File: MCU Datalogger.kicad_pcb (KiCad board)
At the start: 2 copper layers, 29 parts, among them J1 Conn_01x04_Pin, J2 Conn_01x04_Pin, J3 Conn_01x09_Pin, J4 Conn_02x03_Odd_Even, U1 24LC1025, U2 24LC1025, U3 DS1337S_, U4 ATMEGA328P-AU, Y1 32.768 KHz, Y2 16 MHz

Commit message: Completed placements of footprints.
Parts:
- moved H3 129.1 mm to (110.5, 38.1)
- moved C5 128.3 mm to (94.0, 38.1)
- moved R7 122.7 mm to (98.4, 41.9), turned to 180 degrees
- moved C3 121.6 mm to (89.5, 38.1)
- moved D2 120.5 mm to (102.9, 38.1)
- moved BT1 120.1 mm to (69.2, 43.9)
- moved R5 119.0 mm to (102.9, 41.9), turned to 180 degrees
- moved R6 118.2 mm to (102.9, 45.7)
- moved D1 116.6 mm to (98.7, 38.1)
- moved C1 115.0 mm to (85.1, 38.1)
- moved U3 112.5 mm to (77.4, 54.0)
- moved U4 112.4 mm to (89.5, 47.4)
- moved H4 112.4 mm to (110.5, 63.5)
- moved R4 111.0 mm to (98.4, 45.7)
- moved J4 110.8 mm to (107.3, 42.5)
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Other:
- board outline added: 49.3 x 30.5 mm

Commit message: routing sans GND Vcc complete.
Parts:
- moved BT1 0.64 mm to (68.6, 43.9)
- moved Y1 0.64 mm to (68.6, 54.7)
- moved U4 0.63 mm to (88.9, 47.4)
- moved R1 0.57 mm to (73.7, 59.1)
- moved R2 0.57 mm to (77.5, 59.1)
- moved U3 0.57 mm to (76.8, 54.0)
- moved U1 0.57 mm to (76.9, 47.0)
- moved U2 0.57 mm to (76.9, 40.0)
- turned C1 to 180 degrees
- turned C4 to 180 degrees
- turned Y2 to 180 degrees
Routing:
- net /Vcc: track 0.00 -> 130.9 mm, vias 0 -> 5
- net /SCK: track 0.00 -> 95.1 mm
- net /SDA: track 0.00 -> 60.0 mm, vias 0 -> 4
- net GND: track 0.00 -> 59.2 mm, vias 0 -> 5
- net Net-(BT1-+): track 0.00 -> 55.3 mm, vias 0 -> 2
- net /TX: track 0.00 -> 29.9 mm, vias 0 -> 1
- net /D2: track 0.00 -> 29.3 mm
- net /RX: track 0.00 -> 27.0 mm, vias 0 -> 1
- net /MOSI: track 0.00 -> 26.4 mm
- net Net-(U4-PB7): track 0.00 -> 25.2 mm, vias 0 -> 2
- net /MISO: track 0.00 -> 24.3 mm
- net /D3: track 0.00 -> 24.2 mm
- net /RESET: track 0.00 -> 22.7 mm, vias 0 -> 2
- net Net-(U4-PB6): track 0.00 -> 22.5 mm
- net /D4: track 0.00 -> 21.6 mm
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
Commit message: Completed routing.
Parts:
- moved H3 0.64 mm to (111.1, 38.1)
- moved H4 0.64 mm to (111.1, 63.5)
- moved H1 0.31 mm to (66.7, 38.1)
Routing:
- net GND: track 59.2 -> 62.9 mm, vias 5 -> 7
- added copper zone on B.Cu, net GND
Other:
- board size 49.3 x 30.5 mm -> 49.8 x 30.5 mm
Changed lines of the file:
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@@
 		(tags "resistor")
 		(property "Reference" "R5"
-			(at 0 -1.65 0)
+			(at 0.9125 1.81 0)
 			(layer "F.SilkS")
 			(effects
@@
 		(tags "resistor")
 		(property "Reference" "R3"
-			(at 0 -1.65 0)
+			(at -0.675 1.63 0)
 			(layer "F.SilkS")
 			(effects
@@
 		(tags "Through hole pin header THT 1x04 2.54mm single row")
 		(property "Reference" "J1"
-			(at 0 -2.38 0)
+			(at -2.655 -0.85 0)
 			(layer "F.SilkS")
 			(effects
@@
 		(tags "resistor")
 		(property "Reference" "R6"
-			(at 0 -1.65 0)
+			(at -0.615732 -1.92 0)
 			(layer "F.SilkS")
 			(effects
@@
 		(tags "Through hole pin header THT 2x03 2.54mm double row")
 		(property "Reference" "J4"
-			(at 1.27 -2.38 0)
+			(at 0.69 -2.38 0)
 			(layer "F.SilkS")
 			(effects
@@
 	(footprint "MountingHole:MountingHole_2.1mm"
 		(layer "F.Cu")
-		(at 110.49 38.1)
+		(at 111.125 38.1)
 		(descr "Mounting Hole 2.1mm, no annular, generated by kicad-footprint-generator mountinghole.py")
 		(tags "mountinghole")
 		(property "Reference" "H3"
-			(at 0 -3.05 0)
+			(at -3.49 -1.524 0)
 			(layer "F.SilkS")
 			(effects
@@
 		(tags "Through hole pin header THT 1x09 2.54mm single row")
 		(property "Reference" "J3"
-			(at 0 -2.38 90)
+			(at 0 -2.38 180)
 			(layer "F.SilkS")
 			(effects
@@
 	(footprint "MountingHole:MountingHole_2.1mm"
 		(layer "F.Cu")
-		(at 66.675 37.79)
+		(at 66.675 38.1)
 		(descr "Mounting Hole 2.1mm, no annular, generated by kicad-footprint-generator mountinghole.py")
 		(tags "mountinghole")
 		(property "Reference" "H1"
-			(at 0 -3.05 0)
+			(at -1.05 2.91 0)
 			(layer "F.SilkS")
 			(effects
@@
 		(tags "Through hole pin header THT 1x04 2.54mm single row")
 		(property "Reference" "J2"
-			(at 0 -2.38 90)
+			(at 0 -2.38 180)
 			(layer "F.SilkS")
 			(effects
@@
 		(descr "SMD2520/2, Crystal, 5.0x3.2mm package, SMD, hand-soldering, generated with kicad-footprint-generator make_crystal.py, http://www.icbase.com/File/PDF/HKC/HKC00061008.pdf")
 		(property "Reference" "Y1"
-			(at 0 -2.8 90)
+			(at -5.37 0.18 180)
 			(layer "F.SilkS")
 			(effects
@@
 	(footprint "MountingHole:MountingHole_2.1mm"
 		(layer "F.Cu")
-		(at 110.49 63.5)
+		(at 111.125 63.5)
 		(descr "Mounting Hole 2.1mm, no annular, generated by kicad-footprint-generator mountinghole.py")
 		(tags "mountinghole")
 		(property "Reference" "H4"
-			(at 0 -3.05 0)
+			(at -2.49 -2 0)
 			(layer "F.SilkS")
 			(effects
@@
 		(tags "capacitor")
 		(property "Reference" "C1"
-			(at 0 -1.68 0)
+			(at 0.45 1.8 0)
 			(layer "F.SilkS")
 			(effects
@@
 		(tags "SOIC SO P-SOP SOP SOP-8 SO SO-8 8S2 S2AE/F K04-056 CASE-751BE SO8W 8-Pin-SOIC PSA W8-2 W8-4 W8MS-1 FPT-8P-M08")
 		(property "Reference" "U1"
-			(at 0 -3.6 0)
+			(at 0 -3.39 0)
 			(layer "F.SilkS")
 			(effects
@@
 		(at 88.9 47.35)
 		(property "Reference" "U4"
-			(at -2.795 -6.79 0)
+			(at -2.795 -6.25 0)
 			(layer "F.SilkS")
 			(effects
@@
 		(tags "resistor")
 		(property "Reference" "R7"
-			(at 0 -1.65 0)
+			(at 0.4 1.91 0)
 			(layer "F.SilkS")
 			(effects
@@
 		(tags "resistor")
 		(property "Reference" "R4"
-			(at 0 -1.65 0)
+			(at -0.9125 -1.8075 0)
 			(layer "F.SilkS")
 			(effects
@@
 	(gr_rect
 		(start 64.135 35.433)
-		(end 113.411 65.913)
+		(end 113.919 65.913)
 		(stroke
 			(width 0.05)
@@
 	)
 	(segment
+		(start 84.73 46.15)
+		(end 85.886117 46.15)
+		(width 0.35)
+		(layer "F.Cu")
+		(net 1)
+	)
+	(segment
 		(start 84.77 39.37)
 		(end 86.04 38.1)
@@
 	)
 	(segment
+		(start 93.07 46.95)
+		(end 92.295912 46.95)
+		(width 0.35)
+		(layer "F.Cu")
+		(net 1)
+	)
+	(segment
 		(start 68.58 46.41)
 		(end 73.08 41.91)
@@
 	)
 	(segment
+		(start 91.6 46.254088)
+		(end 91.6 45.4)
+		(width 0.35)
+		(layer "F.Cu")
+		(net 1)
+	)
+	(segment
 		(start 74.93 39.37)
 		(end 80.4875 39.37)
@@
 	)
 	(segment
+		(start 92.295912 46.95)
+		(end 91.6 46.254088)
+		(width 0.35)
+		(layer "F.Cu")
+		(net 1)
+	)
+	(segment
 		(start 99.3375 40.3375)
 		(end 99.25 40.25)
@@
 	)
 	(via
+		(at 85.886117 46.15)
+		(size 0.9)
+		(drill 0.4)
+		(layers "F.Cu" "B.Cu")
+		(net 1)
+	)
+	(via
 		(at 96.15 38.05)
 		(size 0.9)
@@
 	)
 	(via
+		(at 91.6 45.4)
+		(size 0.9)
+		(drill 0.4)
+		(layers "F.Cu" "B.Cu")
+		(net 1)
+	)
+	(via
 		(at 75.747501 55.442098)
 		(size 0.9)
@@
 		(net 26)
 	)
+	(zone
+		(net 1)
+		(net_name "GND")
+		(layer "B.Cu")
+		(name "GND")
+		(hatch edge 0.5)
+		(connect_pads
+			(clearance 0.5)
+		)
+		(min_thickness 0.25)
+		(filled_areas_thickness no)
+		(fill yes
+			(mode hatch)
+			(thermal_gap 0.5)
+			(thermal_bridge_width 0.5)
+			(hatch_thickness 1)
+			(hatch_gap 1.5)
+			(hatch_orientation 0)
+			(hatch_border_algorithm hatch_thickness)
+			(hatch_min_hole_area 0.3)
+		)
+		(polygon
+			(pts
+				(xy 66.675 60.325) (xy 66.675 63.5) (xy 66.675 65.278) (xy 66.802 65.278) (xy 69.215 65.278) (xy 107.95 65.278)
+				(xy 107.95 65.278) (xy 109.44 65.278) (xy 111.506 65.278) (xy 111.506 65.278) (xy 111.506 65.278)
+				(xy 111.506 40.894) (xy 111.506 40.894) (xy 111.506 36.576) (xy 110.744 36.576) (xy 109.474 36.576)
+				(xy 107.95 36.576) (xy 69.85 36.576) (xy 67.31 36.576) (xy 66.675 36.576) (xy 66.675 40.64) (xy 66.675 40.64)
+			)
+		)
+	)
 	(embedded_fonts no)

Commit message: Refined routing completed.
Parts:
- moved H1 1.27 mm to (67.9, 38.1)
- moved H2 1.27 mm to (67.9, 63.5)
- moved BT1 0.64 mm to (69.2, 43.9)
- moved Y1 0.64 mm to (69.2, 54.7)
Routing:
- net GND: track 62.9 -> 55.9 mm
- net Net-(U3-X1): track 5.78 -> 5.14 mm
- net Net-(U3-X2): track 7.41 -> 6.77 mm
- net Net-(U3-SQW/~INT): track 7.75 -> 7.18 mm
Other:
- board size 49.8 x 30.5 mm -> 48.3 x 30.5 mm

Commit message: Fixed outstanding issues.
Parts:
- moved H3 0.64 mm to (110.5, 38.1)
- moved H4 0.64 mm to (110.5, 63.5)
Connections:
- BT1 pad 1: Net-(BT1-+) -> /Vcc
- C5 pad 1: Net-(BT1-+) -> /Vcc
- D1 pad 2: Net-(BT1-+) -> /Vcc
- U4 pad 18: Net-(BT1-+) -> /Vcc
- U4 pad 6: VCC_1 -> VCC
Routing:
- net /Vcc: track 131.1 -> 189.9 mm, vias 5 -> 7
- net Net-(BT1-+): track 55.1 -> 0.00 mm, vias 2 -> 0
- net VCC: track 0.00 -> 3.38 mm
- net GND: track 55.9 -> 54.7 mm
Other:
- board size 48.3 x 30.5 mm -> 47.6 x 30.5 mm
- board text added: "- 2Mbit EEPROM - RTC - I2C, SPI, GPIOs"
- board text added: "2"
- board text added: "3"
- board text added: "4"
- board text added: "5"
- board text added: "6"
- board text added: "7"
- board text added: "8"
- board text added: "AISHWARYA DIXIT"
- board text added: "DATA LOGGER WITH THE ATMEGA328P"
- board text added: "GND"
- board text added: "GPIO"
- board text added: "I2C"
- board text added: "ICSP"
- board text added: "ICSP MISO VCC SCK MOSI RESET GND"
- board text added: "Rx"
- board text added: "SCK"
- board text added: "SDA"
- board text added: "SERIAL"
- board text added: "Tx"
- board text added: "VCC"
- board text added: "Vcc"

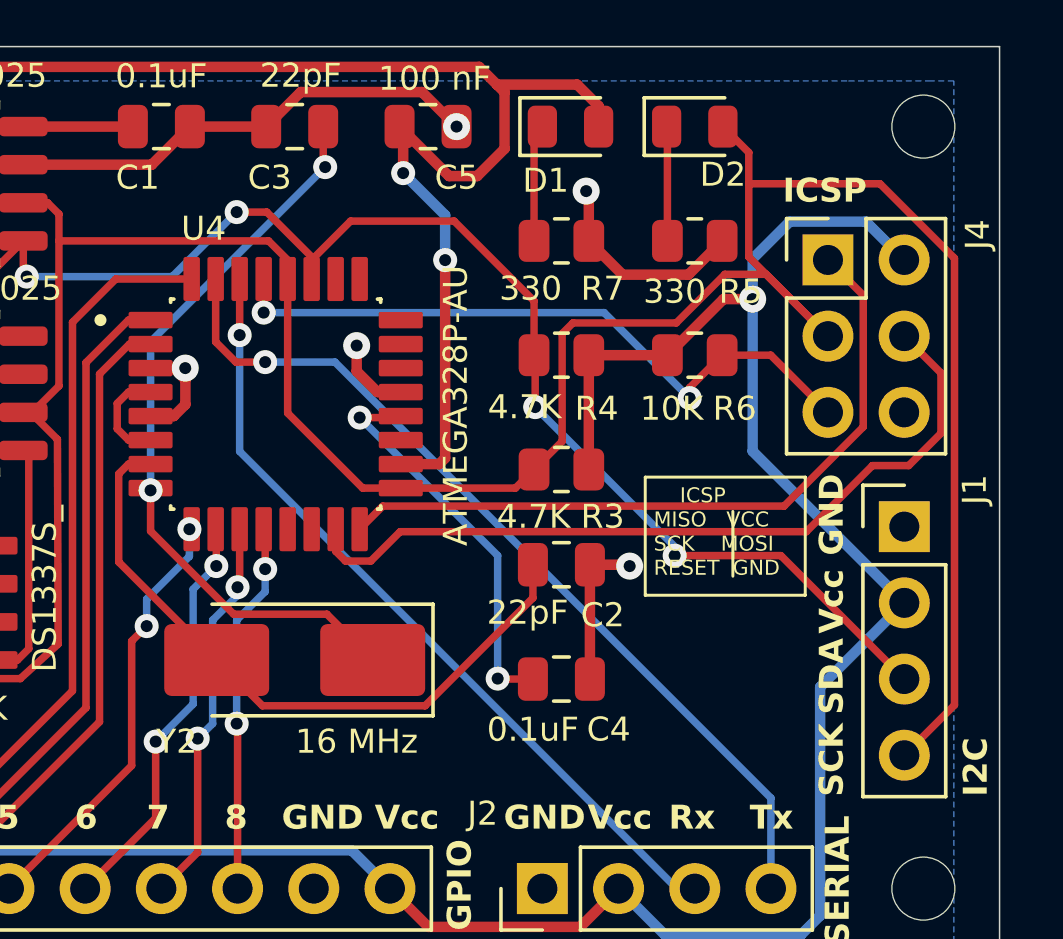
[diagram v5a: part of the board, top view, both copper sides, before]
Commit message: Fixed the defects in 2layer.
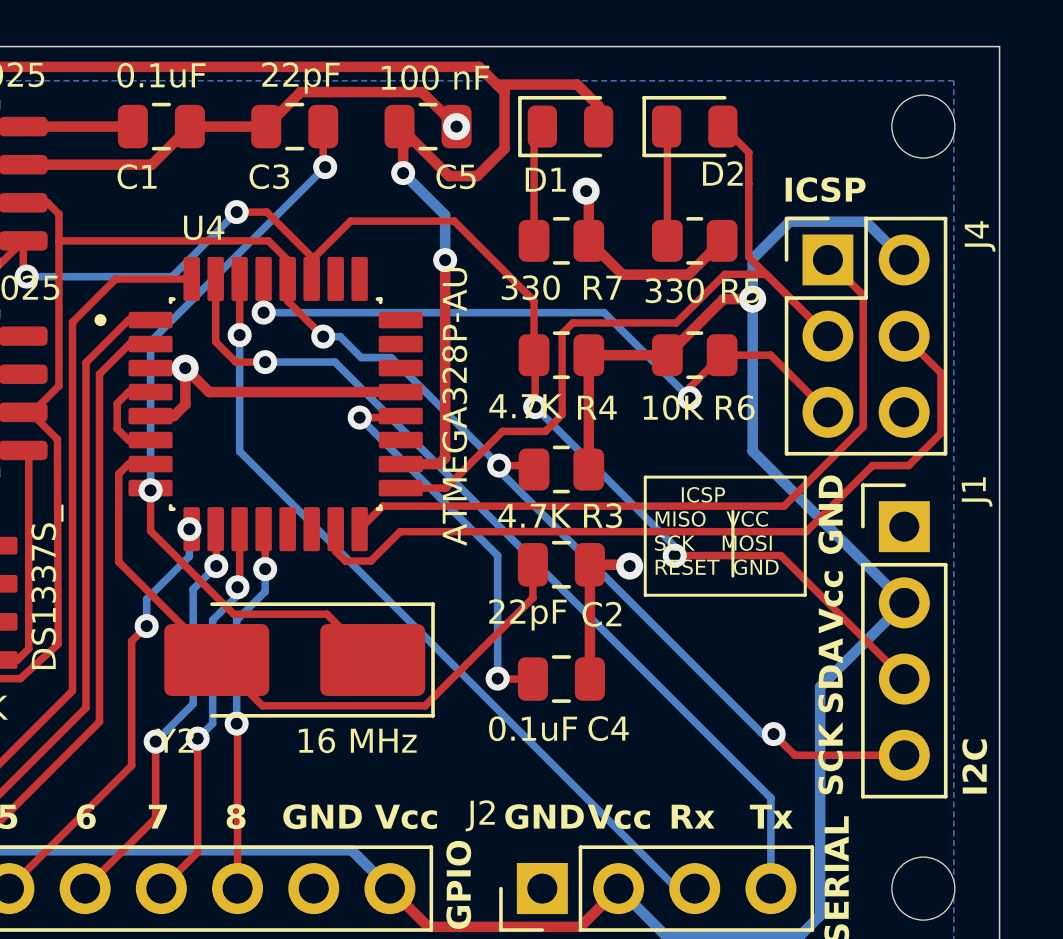
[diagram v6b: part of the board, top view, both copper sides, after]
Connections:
- J1 pad 4: /SCK -> /SCL
- R3 pad 2: /SCK -> /SCL
- U1 pad 6: /SCK -> /SCL
- U2 pad 6: /SCK -> /SCL
- U3 pad 6: /SCK -> /SCL
- U4 pad 28: /SCK -> /SCL
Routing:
- net /SCK: track 95.5 -> 28.1 mm
- net /SCL: track 0.00 -> 61.3 mm, vias 0 -> 3
- net GND: track 54.7 -> 59.6 mm, vias 7 -> 6

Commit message: Completed 2layer.
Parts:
- moved BT1 53.4 mm to (69.2, 97.2)
- moved C1 53.4 mm to (85.1, 91.5)
- moved C3 53.4 mm to (89.5, 91.5)
- moved C5 53.4 mm to (94.0, 91.5)
- moved D1 53.4 mm to (98.7, 91.5)
- moved D2 53.4 mm to (102.9, 91.5)
- moved H1 53.4 mm to (67.9, 91.5)
- moved H3 53.4 mm to (110.5, 91.5)
- moved R1 53.4 mm to (73.7, 112.4)
- moved R2 53.4 mm to (77.5, 112.4)
- moved U1 53.4 mm to (76.9, 100.3)
- moved U2 53.4 mm to (76.9, 93.4)
- moved U3 53.4 mm to (76.8, 107.3)
- moved U4 53.4 mm to (88.9, 100.7)
- moved Y2 53.4 mm to (89.5, 109.2)
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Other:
- board text added: "0.0000 mm / 0.0000 mm"
- board text added: "0.3000 mm"
- board text added: "1.6000 mm"
- board text added: "47.6250 mm x 30.4800 mm"
- board text added: "BOARD CHARACTERISTICS"
- board text added: "Board Thickness:"
- board text added: "Board overall dimensions:"
- board text added: "Castellated pads:"
- board text added: "Copper Finish:"
- board text added: "Copper Layer Count:"
- board text added: "Edge card connectors:"
- board text added: "Impedance Control:"
- board text added: "Min hole diameter:"
- board text added: "Min track/spacing:"
- board text added: "No"
- board text added: "None"
- board text added: "Plated Board Edge:"
